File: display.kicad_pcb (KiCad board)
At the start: 2 copper layers, 151.9 x 30.2 mm, 45 parts, among them P1 USB, P11 NAV_ID, P12 NAV_VOL, P2 Power, P3 SPI Debug, P4 LED_JUMPER, P5 COM_ENC, P6 COM_STEP, P8 COM_VOL, P9 NAV_ENC, U1 ATmega32U4, U10 RESET, U11 COM_TRANS, U12 NAV_TRANS, U2 MAX7221, U3 5x7Segment_0.36, U4 MAX7221, U5 5x7Segment_0.36, U6 MAX7221, U7 5x7Segment_0.36, U8 MAX7221, U9 5x7Segment_0.36

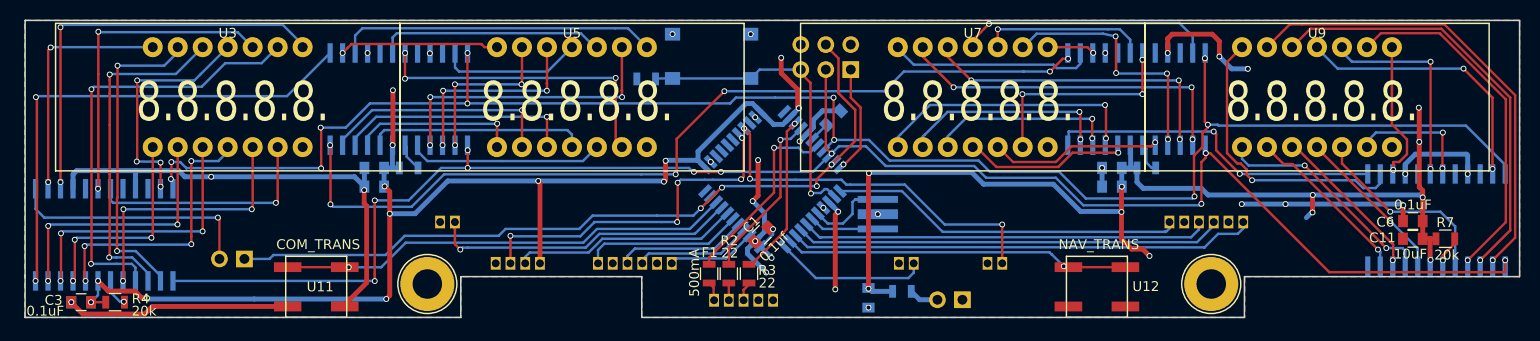
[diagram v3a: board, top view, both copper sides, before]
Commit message: Updated with actual dimensions from 7 segment displays.  Deleted unused files.
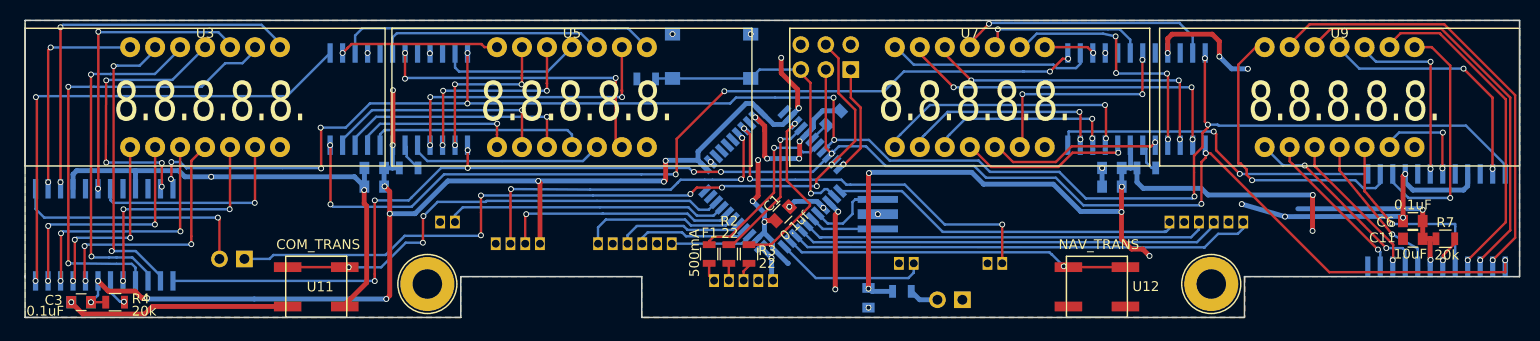
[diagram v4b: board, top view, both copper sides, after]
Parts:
- moved C1 3.01 mm to (177.0, 119.7)
- moved U9 2.30 mm to (233.7, 107.8)
- moved U3 2.30 mm to (118.3, 107.8)
- moved F1 2.00 mm to (169.6, 123.8)
- moved P5 2.00 mm to (162.0, 122.7)
- moved P8 2.00 mm to (150.1, 122.7)
- moved R2 2.00 mm to (171.6, 123.8)
- moved R3 2.00 mm to (173.6, 123.8)
- moved P1 2.00 mm to (173.1, 126.5)
- moved U7 0.30 mm to (196.1, 107.8)
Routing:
- net GND: track 124.5 -> 140.7 mm, vias 25 -> 26
- net /NavStandby/D_5: track 15.3 -> 26.4 mm
- net VCC: track 253.3 -> 244.3 mm, vias 30 -> 27
- net /ComActive/D_2: track 24.0 -> 28.2 mm
- net /NavStandby/S_E: track 23.3 -> 20.4 mm
- net /COM_STEP: track 31.7 -> 28.9 mm, vias 1 -> 0
- net /ComActive/S_B: track 44.5 -> 47.2 mm
- net /ComActive/S_C: track 27.7 -> 25.1 mm, vias 4 -> 3
- net /MOSI: track 79.0 -> 81.5 mm, vias 4 -> 6
- net /NavStandby/D_3: track 21.3 -> 18.9 mm
- net /NavStandby/D_4: track 12.9 -> 10.6 mm
- net /COM_TRANS: track 46.3 -> 48.7 mm, vias 1 -> 3
- net /ComActive/S_D: track 26.7 -> 24.4 mm
- net /ComActive/S_G: track 26.7 -> 24.4 mm
- net /ComActive/D_1: track 24.9 -> 22.6 mm
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
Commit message: Tons of updates.  Mostly working.
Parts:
- added P7: LDR, custom:JST-ZH-THRx2, B.Cu at (196.3, 124.7)
- added R8: 10k, Resistors_SMD:R_0805, B.Cu at (197.0, 118.8)
- moved P12 4.40 mm to (203.0, 124.7)
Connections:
- U1 pad 39: (no net) -> /LDR
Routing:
- net /LDR: track 0.00 -> 45.1 mm, vias 0 -> 5
- net /NAV_VOL: track 36.9 -> 41.4 mm
- net VCC: track 244.3 -> 246.6 mm
- net CS: track 175.0 -> 176.1 mm
